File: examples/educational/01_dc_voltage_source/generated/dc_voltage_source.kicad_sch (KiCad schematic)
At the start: 3 parts, among them J1 9 V OUTPUT

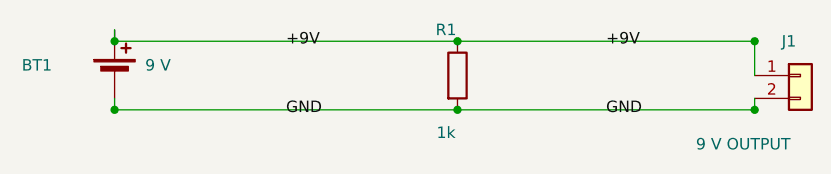
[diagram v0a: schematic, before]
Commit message: feat: infer conventional schematic topology layouts
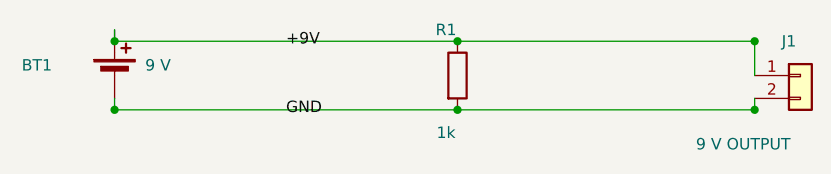
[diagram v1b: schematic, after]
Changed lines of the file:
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@@
-  )
-  (label
-    "+9V"
-    (at 163.83 100.33 0)
-    (effects
-      (font
-        (size 1.27 1.27)
-      )
-    )
   )
   (label
@@
     (effects
       (font
-        (size 1.27 1.27)
-      )
-    )
-  )
-  (label
-    "GND"
-    (at 163.83 107.95 0)
-    (effects
-      (font
